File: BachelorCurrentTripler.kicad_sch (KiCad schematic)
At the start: 0 parts

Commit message: addded phaseA
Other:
- added sheet PhaseA (PhaseA.kicad_sch)
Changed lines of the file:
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@@
 	(paper "A4")
 	(sheet
-		(at 115.57 86.36)
+		(at 133.35 36.83)
+		(size 38.1 25.4)
+		(exclude_from_sim no)
+		(in_bom yes)
+		(on_board yes)
+		(dnp no)
+		(fields_autoplaced yes)
+		(stroke
+			(width 0.1524)
+			(type solid)
+		)
+		(fill
+			(color 0 0 0 0.0000)
+		)
+		(property "Sheetname" "PhaseA"
+			(at 133.35 36.1184 0)
+			(effects
+				(font
+					(size 1.27 1.27)
+				)
+				(justify left bottom)
+			)
+		)
+		(property "Sheetfile" "PhaseA.kicad_sch"
+			(at 133.35 62.8146 0)
+			(effects
+				(font
+					(size 1.27 1.27)
+				)
+				(justify left top)
+			)
+		)
+		(instances
+			(project "BachelorCurrentTripler"
+				(path "/eaeaab39-7712-4bb8-8f1a-3ddca096a313"
+					(page "3")
+				)
+			)
+		)
+	)
+	(sheet
+		(at 40.64 66.04)
 		(size 55.88 31.75)
 		(exclude_from_sim no)
@@
 		)
 		(property "Sheetname" "CurrentTriplerMainCircuit"
-			(at 115.57 85.6484 0)
+			(at 40.64 65.3284 0)
 			(effects
 				(font
@@
 		)
 		(property "Sheetfile" "01_MainCircuitry.kicad_sch"
-			(at 115.57 118.6946 0)
+			(at 40.64 98.3746 0)
 			(effects
 				(font

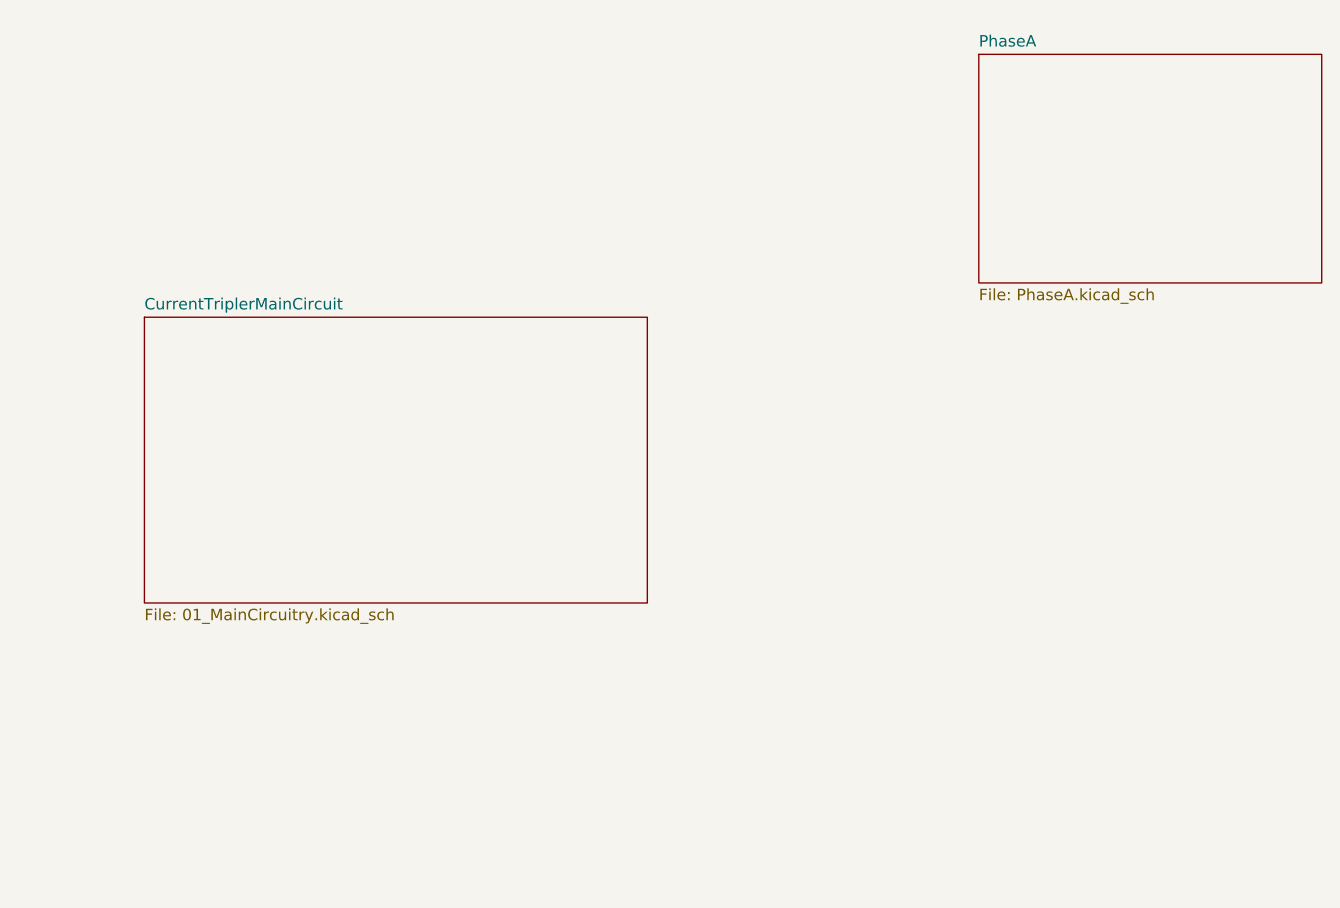
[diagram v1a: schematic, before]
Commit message: added hirearchical labels
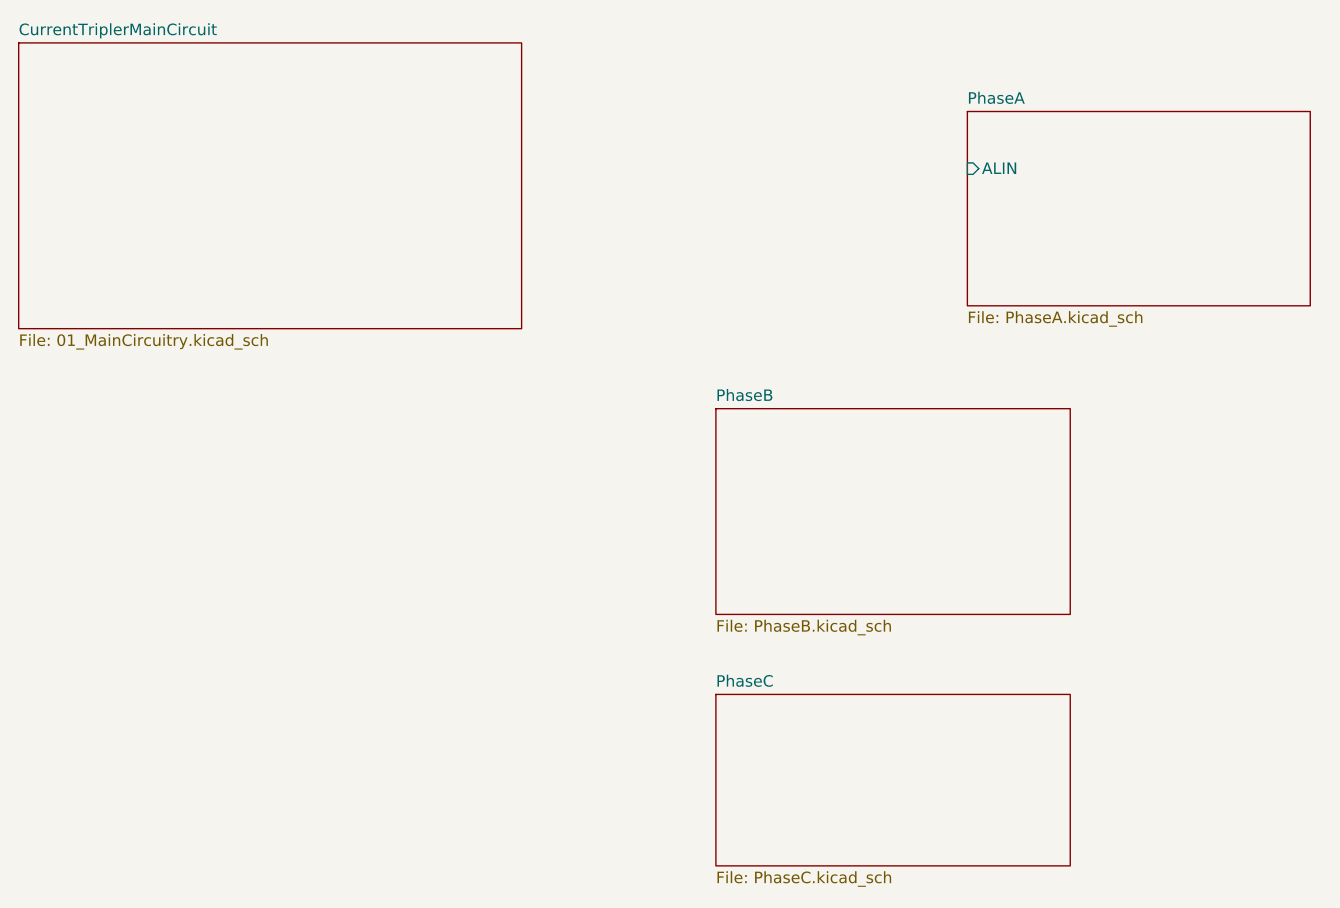
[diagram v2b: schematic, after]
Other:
- added sheet PhaseB (PhaseB.kicad_sch)
- added sheet PhaseC (PhaseC.kicad_sch)
- sheet PhaseA ports: added ALIN; removed none
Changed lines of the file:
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@@
 	(paper "A4")
 	(sheet
-		(at 133.35 36.83)
-		(size 38.1 25.4)
+		(at 104.14 76.2)
+		(size 39.37 22.86)
+		(exclude_from_sim no)
+		(in_bom yes)
+		(on_board yes)
+		(dnp no)
+		(fields_autoplaced yes)
+		(stroke
+			(width 0.1524)
+			(type solid)
+		)
+		(fill
+			(color 0 0 0 0.0000)
+		)
+		(property "Sheetname" "PhaseB"
+			(at 104.14 75.4884 0)
+			(effects
+				(font
+					(size 1.27 1.27)
+				)
+				(justify left bottom)
+			)
+		)
+		(property "Sheetfile" "PhaseB.kicad_sch"
+			(at 104.14 99.6446 0)
+			(effects
+				(font
+					(size 1.27 1.27)
+				)
+				(justify left top)
+			)
+		)
+		(instances
+			(project "BachelorCurrentTripler"
+				(path "/eaeaab39-7712-4bb8-8f1a-3ddca096a313"
+					(page "4")
+				)
+			)
+		)
+	)
+	(sheet
+		(at 132.08 43.18)
+		(size 38.1 21.59)
 		(exclude_from_sim no)
 		(in_bom yes)
@@
 		)
 		(property "Sheetname" "PhaseA"
-			(at 133.35 36.1184 0)
+			(at 132.08 42.4684 0)
 			(effects
 				(font
@@
 		)
 		(property "Sheetfile" "PhaseA.kicad_sch"
-			(at 133.35 62.8146 0)
+			(at 132.08 65.3546 0)
 			(effects
 				(font
@@
 				)
 				(justify left top)
+			)
+		)
+		(pin "ALIN" input
+			(at 132.08 49.53 180)
+			(effects
+				(font
+					(size 1.27 1.27)
+				)
+				(justify left)
 			)
 		)
@@
 	)
 	(sheet
-		(at 40.64 66.04)
+		(at 104.14 107.95)
+		(size 39.37 19.05)
+		(exclude_from_sim no)
+		(in_bom yes)
+		(on_board yes)
+		(dnp no)
+		(fields_autoplaced yes)
+		(stroke
+			(width 0.1524)
+			(type solid)
+		)
+		(fill
+			(color 0 0 0 0.0000)
+		)
+		(property "Sheetname" "PhaseC"
+			(at 104.14 107.2384 0)
+			(effects
+				(font
+					(size 1.27 1.27)
+				)
+				(justify left bottom)
+			)
+		)
+		(property "Sheetfile" "PhaseC.kicad_sch"
+			(at 104.14 127.5846 0)
+			(effects
+				(font
+					(size 1.27 1.27)
+				)
+				(justify left top)
+			)
+		)
+		(instances
+			(project "BachelorCurrentTripler"
+				(path "/eaeaab39-7712-4bb8-8f1a-3ddca096a313"
+					(page "5")
+				)
+			)
+		)
+	)
+	(sheet
+		(at 26.67 35.56)
 		(size 55.88 31.75)
 		(exclude_from_sim no)
@@
 		)
 		(property "Sheetname" "CurrentTriplerMainCircuit"
-			(at 40.64 65.3284 0)
+			(at 26.67 34.8484 0)
 			(effects
 				(font
@@
 		)
 		(property "Sheetfile" "01_MainCircuitry.kicad_sch"
-			(at 40.64 98.3746 0)
+			(at 26.67 67.8946 0)
 			(effects
 				(font

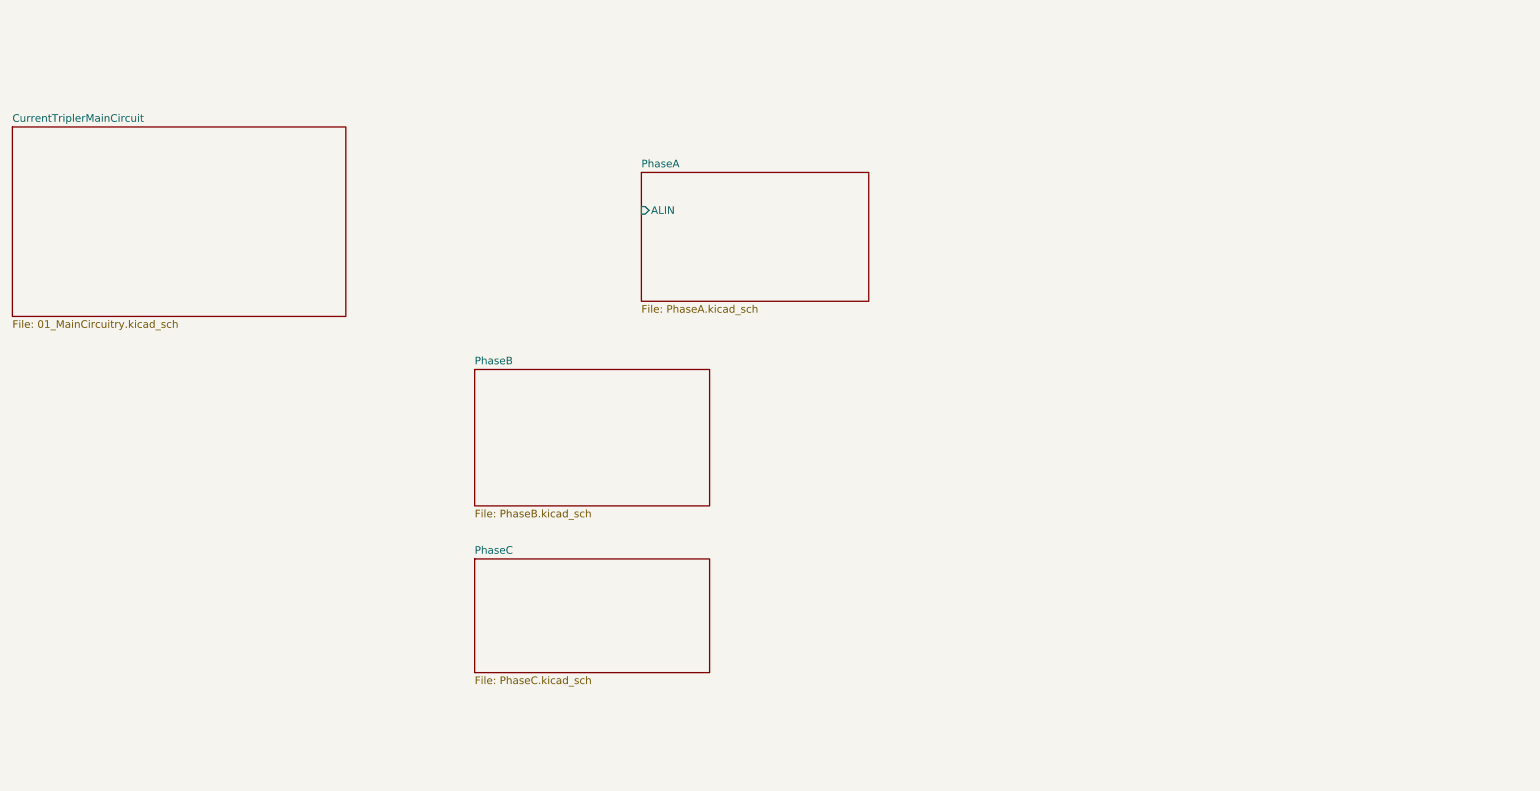
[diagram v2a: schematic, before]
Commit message: added more data for the 3 Phases. also added transformer
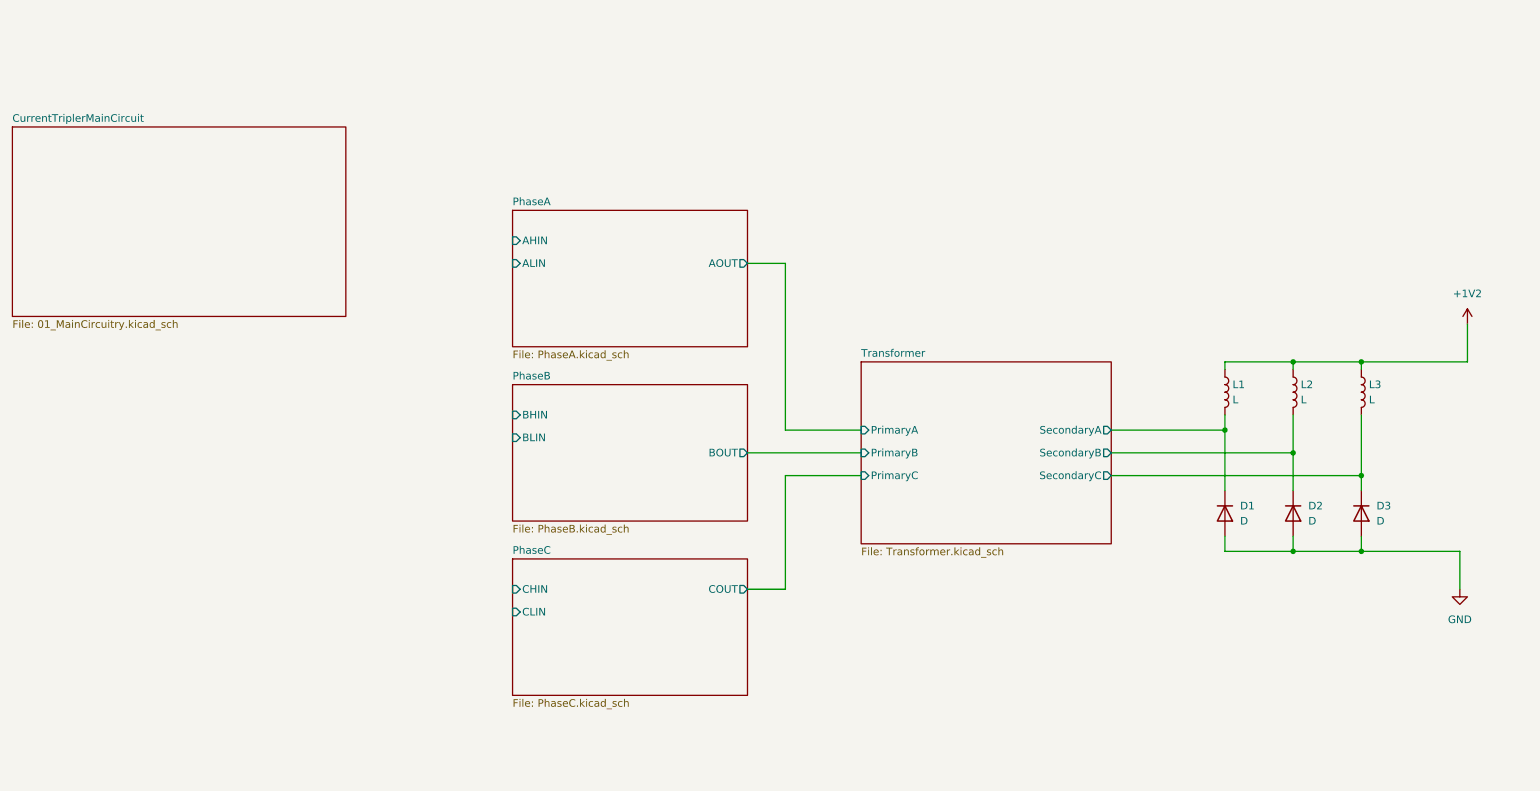
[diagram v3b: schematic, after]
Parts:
- added D1, D2, D3: D, symbol Device:D
- added L1, L2, L3: L, symbol Device:L
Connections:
- new net +1V2: L1.1, L2.1, L3.1
- new net GND: D1.2 (A), D2.2 (A), D3.2 (A)
- new net Transformer/SecondaryA: D1.1 (K), L1.2
- new net Transformer/SecondaryB: D2.1 (K), L2.2
- new net Transformer/SecondaryC: D3.1 (K), L3.2
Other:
- added sheet Transformer (Transformer.kicad_sch)
- sheet PhaseA ports: added AHIN, AOUT; removed none
- sheet PhaseB ports: added BHIN, BLIN, BOUT; removed none
- sheet PhaseC ports: added CHIN, CLIN, COUT; removed none

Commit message: added some kind of PCB design, a rough draft
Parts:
- D1, D2, D3: footprint (none) -> Diode_THT:D_5W_P10.16mm_Horizontal
- L1, L2, L3: footprint (none) -> Inductor_THT:L_Axial_L11.0mm_D4.5mm_P15.24mm_Horizontal_Fastron_MECC
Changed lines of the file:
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@@
 			)
 		)
-		(property "Footprint" ""
+		(property "Footprint" "Diode_THT:D_5W_P10.16mm_Horizontal"
 			(at 229.87 100.33 0)
 			(effects
@@
 			)
 		)
-		(property "Footprint" ""
+		(property "Footprint" "Diode_THT:D_5W_P10.16mm_Horizontal"
 			(at 241.3 100.33 0)
 			(effects
@@
 			)
 		)
-		(property "Footprint" ""
+		(property "Footprint" "Inductor_THT:L_Axial_L11.0mm_D4.5mm_P15.24mm_Horizontal_Fastron_MECC"
 			(at 229.87 80.01 0)
 			(effects
@@
 			)
 		)
-		(property "Footprint" ""
+		(property "Footprint" "Diode_THT:D_5W_P10.16mm_Horizontal"
 			(at 252.73 100.33 0)
 			(effects
@@
 		(dnp no)
 		(fields_autoplaced yes)
-		(property "Reference" "#PWR034"
+		(property "Reference" "#PWR01"
 			(at 270.51 72.39 0)
 			(effects
@@
 			(project "BachelorCurrentTripler"
 				(path "/eaeaab39-7712-4bb8-8f1a-3ddca096a313"
-					(reference "#PWR034")
+					(reference "#PWR01")
 					(unit 1)
 				)
@@
 		(dnp no)
 		(fields_autoplaced yes)
-		(property "Reference" "#PWR018"
+		(property "Reference" "#PWR02"
 			(at 269.24 119.38 0)
 			(effects
@@
 			(project "BachelorCurrentTripler"
 				(path "/eaeaab39-7712-4bb8-8f1a-3ddca096a313"
-					(reference "#PWR018")
+					(reference "#PWR02")
 					(unit 1)
 				)
@@
 			)
 		)
-		(property "Footprint" ""
+		(property "Footprint" "Inductor_THT:L_Axial_L11.0mm_D4.5mm_P15.24mm_Horizontal_Fastron_MECC"
 			(at 241.3 80.01 0)
 			(effects
@@
 			)
 		)
-		(property "Footprint" ""
+		(property "Footprint" "Inductor_THT:L_Axial_L11.0mm_D4.5mm_P15.24mm_Horizontal_Fastron_MECC"
 			(at 252.73 80.01 0)
 			(effects

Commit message: intial pcb layout
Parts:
- added J1: Conn_01x07_Pin, Connector_JST:JST_EH_B7B-EH-A_1x07_P2.50mm_Vertical, symbol Connector:Conn_01x07_Pin
- added J2, J3, J5: Conn_01x01_Pin, Connector_Wire:SolderWirePad_1x01_SMD_5x10mm, symbol Connector:Conn_01x01_Pin
- added J4: Conn_01x04_Socket, Connector_Hirose:Hirose_DF63M-4P-3.96DSA_1x04_P3.96mm_Vertical, symbol Connector:Conn_01x04_Socket
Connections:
- net GND: now also J1.7 (Pin_7), J4.1 (Pin_1), J5.1 (Pin_1)
- net PhaseA/AHIN: now also J1.2 (Pin_2)
- net PhaseA/ALIN: now also J1.1 (Pin_1)
- net PhaseA/AOUT: now also J4.2 (Pin_2)
- net PhaseB/BHIN: now also J1.4 (Pin_4)
- net PhaseB/BLIN: now also J1.3 (Pin_3)
- net PhaseB/BOUT: now also J4.3 (Pin_3)
- net PhaseC/CHIN: now also J1.6 (Pin_6)
- net PhaseC/CLIN: now also J1.5 (Pin_5)
- net PhaseC/COUT: now also J4.4 (Pin_4)
- new net +12V: J3.1 (Pin_1)
- new net +48V: J2.1 (Pin_1)

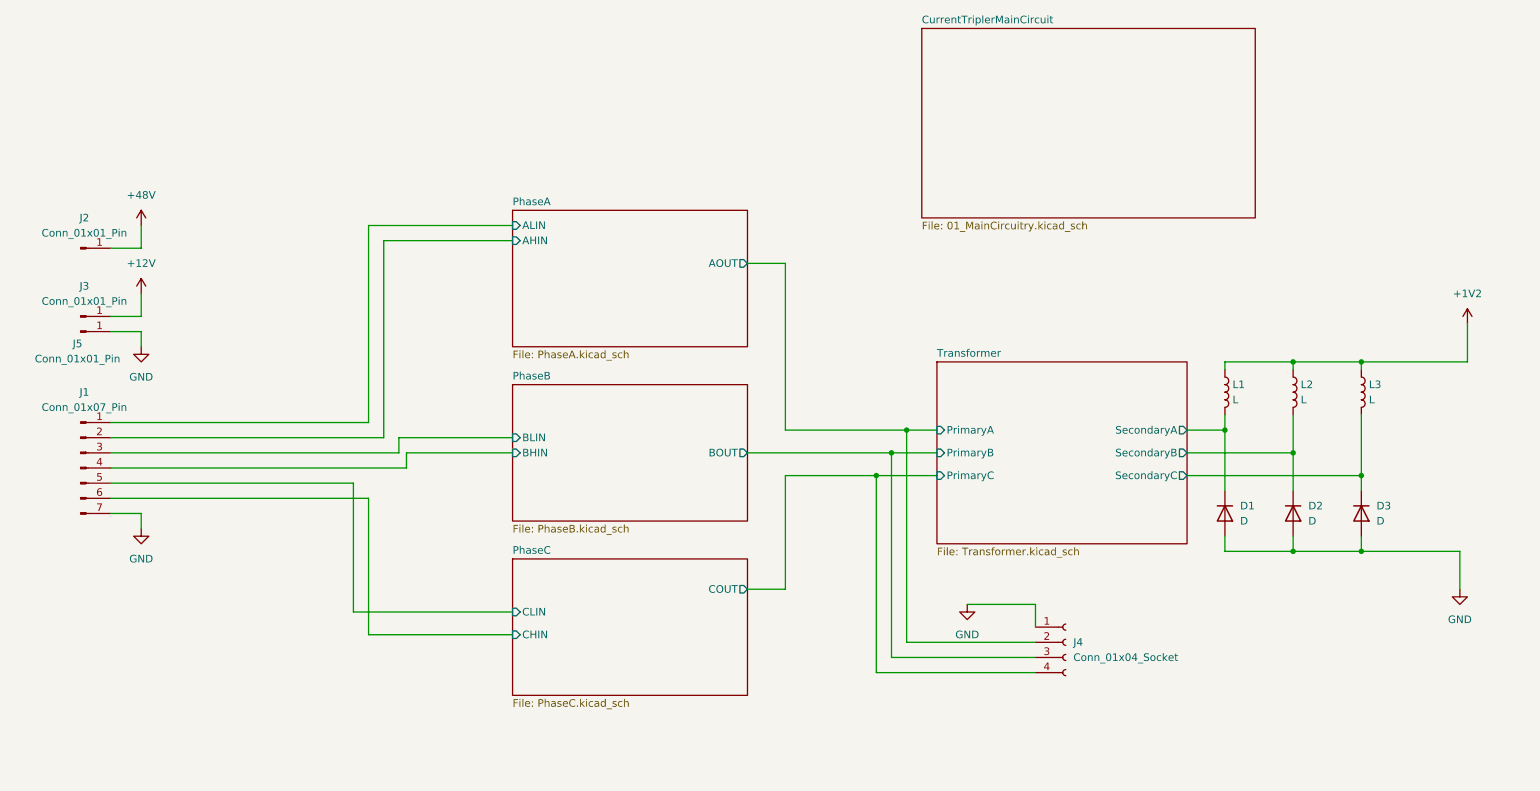
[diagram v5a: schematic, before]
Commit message: Updates to Secondary side for PCB
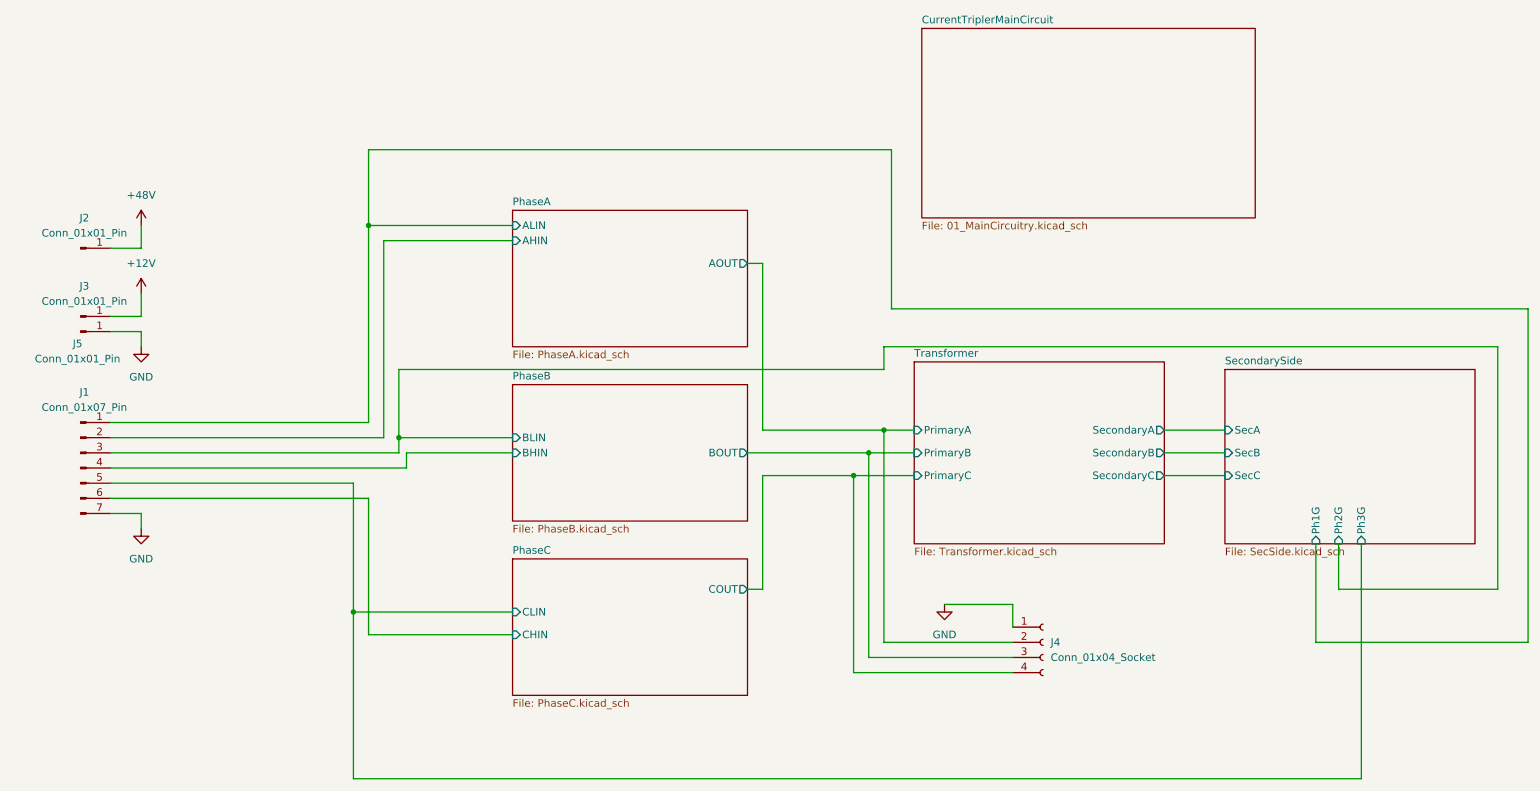
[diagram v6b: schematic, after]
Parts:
- removed D1, D2, D3: D, Diode_THT:D_5W_P10.16mm_Horizontal, symbol Device:D
- removed L1, L2, L3: L, Inductor_THT:L_Axial_L11.0mm_D4.5mm_P15.24mm_Horizontal_Fastron_MECC, symbol Device:L
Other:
- added sheet SecondarySide (SecSide.kicad_sch)
- moved on the sheet: J4
